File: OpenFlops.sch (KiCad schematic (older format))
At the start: 82 parts, among them J99 OSHW_LOGO, P1 FLOPPY_CONN, P2 POWER_INPUT, P3 USB_A_FEMALE, P4 PROG_PORT, P5 JUMPERS, P6 ENCODER_PORT, P7 DISPLAY_PORT, P8 USB_HEADER, P9 EXTERNAL_SPEAKER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

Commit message: Fix #4
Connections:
- net GND: now also U3.28 (PB2)
- no-connect marks 22 -> 21
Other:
- moved on the sheet: P9
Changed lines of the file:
@@
 NoConn ~ 3255 1900
 NoConn ~ 3255 2600
-NoConn ~ 3255 3200
 NoConn ~ 1855 2800
 NoConn ~ 1855 3900
@@
 L Connector_Generic:Conn_01x02 P9
 U 1 1 5D86073A
-P 4235 3670
-F 0 "P9" H 4153 3887 50  0000 C CNN
-F 1 "EXTERNAL_SPEAKER" H 4153 3796 50  0000 C CNN
-F 2 "OpenFlops:PinHeader_1x02_P2.54mm_Mute" H 4235 3670 50  0001 C CNN
-F 3 "~" H 4235 3670 50  0001 C CNN
-	1    4235 3670
+P 4235 3755
+F 0 "P9" H 4153 3972 50  0000 C CNN
+F 1 "EXTERNAL_SPEAKER" H 4153 3881 50  0000 C CNN
+F 2 "OpenFlops:PinHeader_1x02_P2.54mm_Mute" H 4235 3755 50  0001 C CNN
+F 3 "~" H 4235 3755 50  0001 C CNN
+	1    4235 3755
 	-1   0    0    -1
 $EndComp
 Wire Wire Line
-	4435 3670 4680 3670
-Wire Wire Line
-	4435 3770 4680 3770
+	4435 3755 4680 3755
+Wire Wire Line
+	4435 3855 4680 3855
 Wire Wire Line
 	4650 4435 4650 4395
@@
 Text Label 4650 4435 0    50   ~ 0
 spk-
-Text Label 4680 3770 2    50   ~ 0
+Text Label 4680 3855 2    50   ~ 0
 spk-
 Text Label 4650 4060 0    50   ~ 0
 spk+
-Text Label 4680 3670 2    50   ~ 0
+Text Label 4680 3755 2    50   ~ 0
 spk+
 Text Label 7495 1050 0    50   ~ 0
@@
 	0    1    1    0
 $EndComp
+Text Label 3820 3200 2    50   ~ 0
+boot1
+$Comp
+L power:GND #PWR?
+U 1 1 5E2952AE
+P 3950 3250
+F 0 "#PWR?" H 3950 3000 50  0001 C CNN
+F 1 "GND" H 3955 3077 50  0000 C CNN
+F 2 "" H 3950 3250 50  0001 C CNN
+F 3 "" H 3950 3250 50  0001 C CNN
+	1    3950 3250
+	1    0    0    -1
+$EndComp
+Wire Wire Line
+	3950 3200 3950 3250
+Wire Wire Line
+	3255 3200 3950 3200
 $EndSCHEMATC

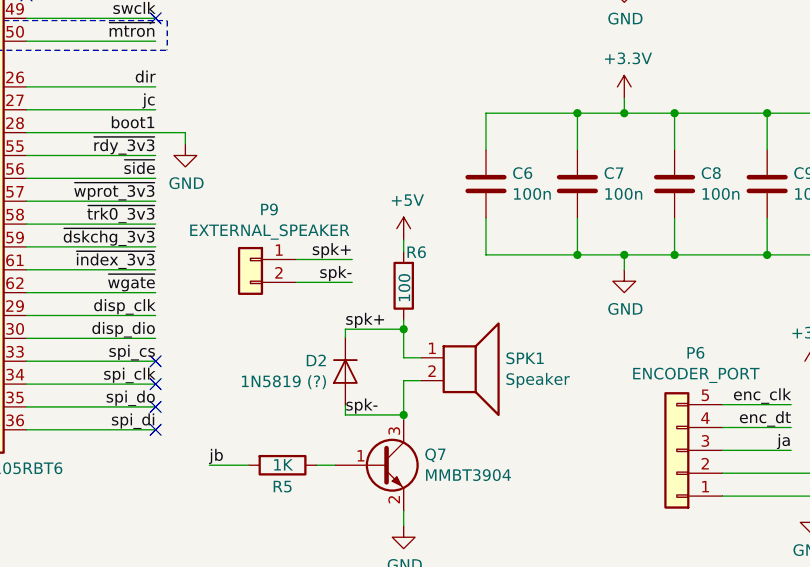
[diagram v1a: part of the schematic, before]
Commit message: Make R6 22R
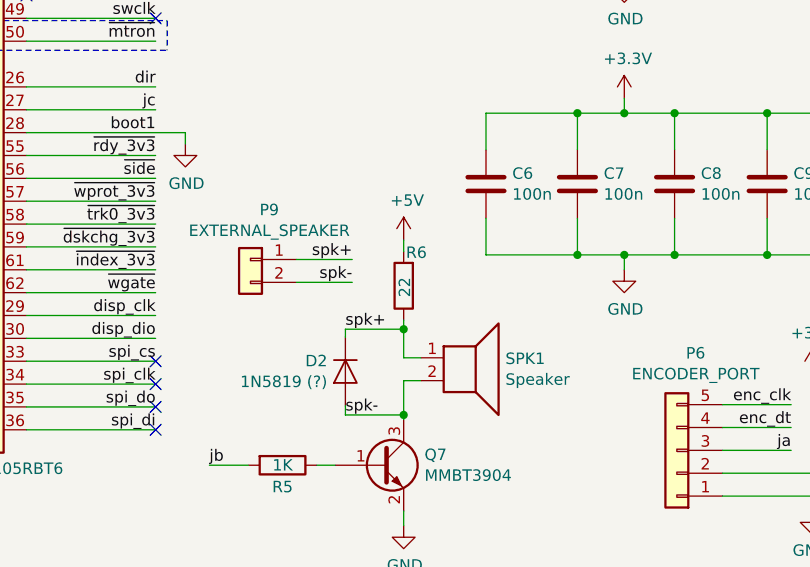
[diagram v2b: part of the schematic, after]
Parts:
- R6: value 100 -> 22
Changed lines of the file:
@@
 P 4905 3870
 F 0 "R6" H 4895 3725 50  0000 R CNN
-F 1 "100" V 4900 3945 50  0000 R CNN
+F 1 "22" V 4900 3920 50  0000 R CNN
 F 2 "Resistor_SMD:R_0805_2012Metric_Pad1.15x1.40mm_HandSolder" V 4835 3870 50  0001 C CNN
 F 3 "~" H 4905 3870 50  0001 C CNN
@@
 boot1
 $Comp
-L power:GND #PWR?
+L power:GND #PWR0146
 U 1 1 5E2952AE
 P 3950 3250
-F 0 "#PWR?" H 3950 3000 50  0001 C CNN
+F 0 "#PWR0146" H 3950 3000 50  0001 C CNN
 F 1 "GND" H 3955 3077 50  0000 C CNN
 F 2 "" H 3950 3250 50  0001 C CNN

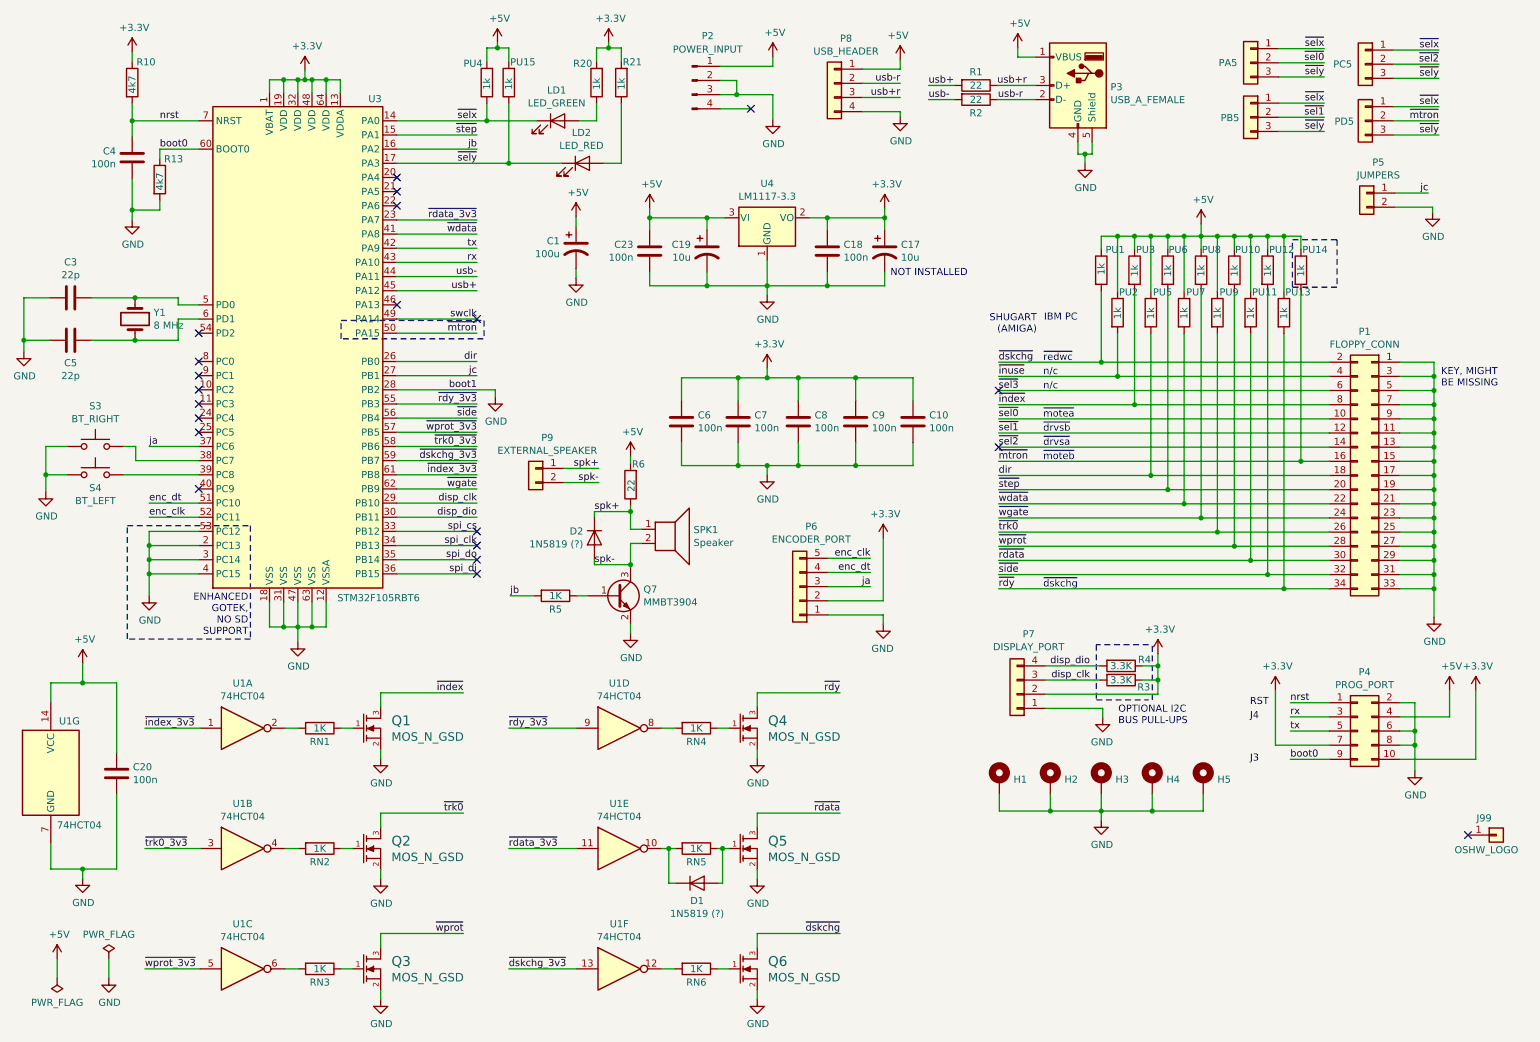
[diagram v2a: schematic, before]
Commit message: Add BOOT1 testpoint and lots of changes for auto P&P
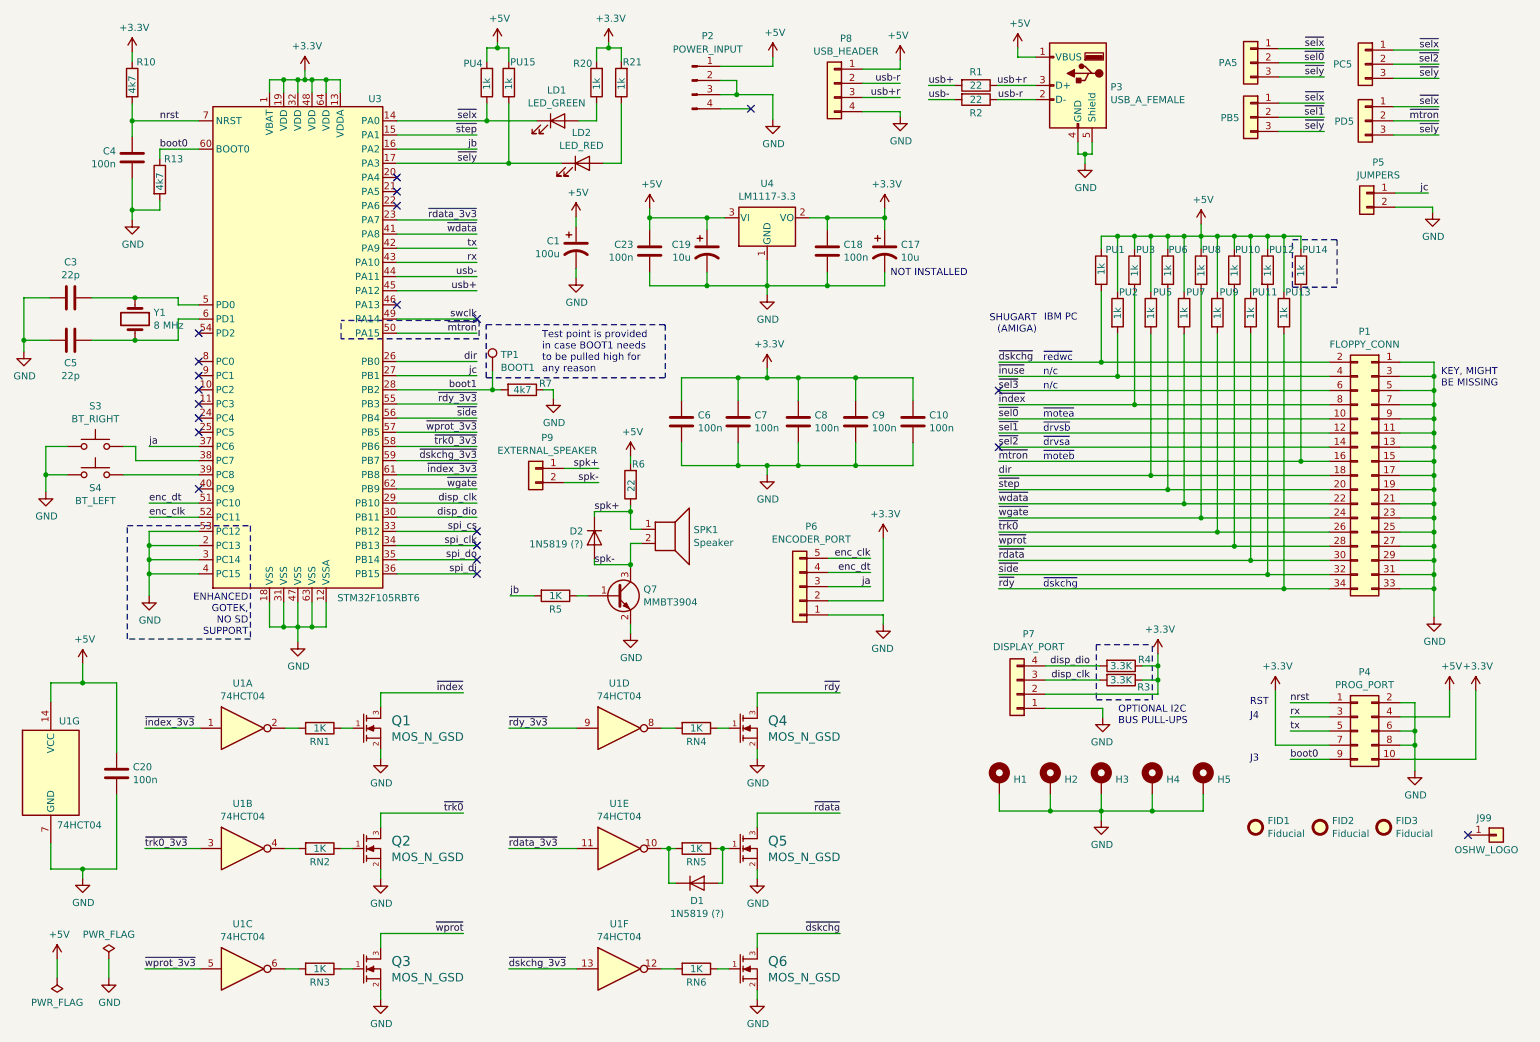
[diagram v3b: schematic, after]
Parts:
- added FID1, FID2, FID3: Fiducial, Fiducial:Fiducial_0.75mm_Mask1.5mm, symbol Mechanical:Fiducial
- added R7: 4k7, Resistor_SMD:R_0805_2012Metric_Pad1.15x1.40mm_HandSolder, symbol Device:R
- added TP1: BOOT1, TestPoint:TestPoint_Pad_D1.5mm, symbol Connector:TestPoint
- C10, C18, C20, C23, C4, C6, C7, C8, C9: JLCPCB PN (none) -> CC0805KRX7R9BB104; MFG Name (none) -> YAGEO; MFG Part Num (none) -> MULTILAYER CERAMIC CAPACITORS MLCC - SMD/SMT 100NF 50V 0805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
- C3, C5: JLCPCB PN (none) -> CL21C220JBANNNC; MFG Name (none) -> SAMSUNG ELECTRO-MECHANICS; MFG Part Num (none) -> MULTILAYER CERAMIC CAPACITORS MLCC - SMD/SMT 22PF 50V 0805 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
- D1, D2: JLCPCB PN (none) -> 1N4148WS; MFG Name (none) -> CHANGJIANG ELECTRONICS TECH (CJ); MFG Part Num (none) -> SWITCHING DIODE 100V 150MA 1.25V @ 150MA 4NS SOD-323 ROHS B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
- PU1, PU10, PU11, PU12, PU13, PU14, PU15, PU2, PU3, PU4, PU5, PU6, PU7, PU8, PU9, RN1, RN2, RN3, RN4, RN5, RN6: JLCPCB PN (none) -> 0805W8F1001T5E; MFG Name (none) -> UNIROYAL ELEC; MFG Part Num (none) -> CHIP RESISTOR - SURFACE MOUNT 1KOHMS ±1% 1/8W 0805 ROHS Bas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
- Q1, Q2, Q3, Q4, Q5, Q6: JLCPCB PN (none) -> BSS138; MFG Name (none) -> ON SEMICON; MFG Part Num (none) -> MOSFET N TRENCH 50V 220MA 1.5V @ 1MA 3.5 ? @ 220MA,10V SOT-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
- Q7: JLCPCB PN (none) -> MMBT3904; MFG Name (none) -> CHANGJIANG ELECTRONICS TECH (CJ); MFG Part Num (none) -> TRANSISTORS (NPN/PNP) NPN 200MA 40V SOT-23(SOT-23-3) ROHS B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
- R1, R2, R6: JLCPCB PN (none) -> 0805W8F220JT5E; MFG Name (none) -> UNIROYAL ELEC; MFG Part Num (none) -> CHIP RESISTOR - SURFACE MOUNT 22OHMS ±1% 1/8W 0805 ROHS Bas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
- R10, R13: JLCPCB PN (none) -> 0805W8F4701T5E; MFG Name (none) -> UNIROYAL ELEC; MFG Part Num (none) -> CHIP RESISTOR - SURFACE MOUNT 4.7KOHMS ±1% 1/8W 0805 ROHS
- U1: JLCPCB PN (none) -> 74HCT04D; MFG Name (none) -> NEXPERIA; MFG Part Num (none) -> GATES AND INVERTERS SOIC-14_150MIL ROHS Extended Part
- U3: JLCPCB PN (none) -> STM32F105RBT6; MFG Name (none) -> STMICROELECTRONICS; MFG Part Num (none) -> ST MICROELECTRONICS LQFP-64_10X10X05P ROHS Extended Part
- U4: JLCPCB PN (none) -> AMS1117-3.3; MFG Name (none) -> ADVANCED MONOLITHIC SYSTEMS; MFG Part Num (none) -> LOW DROPOUT REGULATORS(LDO) POSITIVE FIXED 1.3V @ 800MA 15V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
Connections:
- net GND: now also R7.1; no longer U3.28 (PB2)
- new net boot1: R7.2, TP1.1, U3.28 (PB2)
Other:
- note added: "Test point is provided\nin case BOOT1 needs\nto be pulled high for\nany reason"

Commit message: Some refinements
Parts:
- TP1: footprint TestPoint:TestPoint_Pad_D1.5mm -> TestPoint:TestPoint_Pad_D1.0mm
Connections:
- no-connect marks 21 -> 20
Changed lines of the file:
@@
 	7505 3005 8230 3005
 NoConn ~ 7505 3205
-NoConn ~ 7505 3605
 Text Notes 7820 3105 0    50   ~ 0
 n/c
@@
 F 0 "TP1" H 3988 3188 50  0000 L CNN
 F 1 "BOOT1" H 3988 3097 50  0000 L CNN
-F 2 "TestPoint:TestPoint_Pad_D1.5mm" H 4130 3070 50  0001 C CNN
+F 2 "TestPoint:TestPoint_Pad_D1.0mm" H 4130 3070 50  0001 C CNN
 F 3 "~" H 4130 3070 50  0001 C CNN
 	1    3930 3070

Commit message: Fixes for BOM
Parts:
- D1, D2: value 1N5819 (?) -> 1N4148
- P5: value JUMPERS -> JUMPER_JC
- Q1, Q2, Q3, Q4, Q5, Q6: value MOS_N_GSD -> BSS138
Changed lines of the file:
@@
 P 5375 6685
 F 0 "D1" H 5375 6561 50  0000 C CNN
-F 1 "1N5819 (?)" H 5375 6470 50  0000 C CNN
+F 1 "1N4148" H 5375 6470 50  0000 C CNN
 F 2 "Diode_SMD:D_SOD-323_HandSoldering" H 5375 6685 50  0001 C CNN
 F 3 "~" H 5375 6685 50  0001 C CNN
@@
 P 3040 5590
 F 0 "Q1" H 3216 5643 70  0000 L CNN
-F 1 "MOS_N_GSD" H 3216 5529 60  0000 L CNN
+F 1 "BSS138" H 3216 5529 60  0000 L CNN
 F 2 "Package_TO_SOT_SMD:SOT-23_Handsoldering" H 3040 5590 60  0001 C CNN
 F 3 "" H 3040 5590 60  0000 C CNN
@@
 P 3040 6440
 F 0 "Q2" H 3216 6493 70  0000 L CNN
-F 1 "MOS_N_GSD" H 3216 6379 60  0000 L CNN
+F 1 "BSS138" H 3216 6379 60  0000 L CNN
 F 2 "Package_TO_SOT_SMD:SOT-23_Handsoldering" H 3040 6440 60  0001 C CNN
 F 3 "" H 3040 6440 60  0000 C CNN
@@
 P 3040 7290
 F 0 "Q3" H 3216 7343 70  0000 L CNN
-F 1 "MOS_N_GSD" H 3216 7229 60  0000 L CNN
+F 1 "BSS138" H 3216 7229 60  0000 L CNN
 F 2 "Package_TO_SOT_SMD:SOT-23_Handsoldering" H 3040 7290 60  0001 C CNN
 F 3 "" H 3040 7290 60  0000 C CNN
@@
 P 5700 7290
 F 0 "Q6" H 5876 7343 70  0000 L CNN
-F 1 "MOS_N_GSD" H 5876 7229 60  0000 L CNN
+F 1 "BSS138" H 5876 7229 60  0000 L CNN
 F 2 "Package_TO_SOT_SMD:SOT-23_Handsoldering" H 5700 7290 60  0001 C CNN
 F 3 "" H 5700 7290 60  0000 C CNN
@@
 P 5700 6440
 F 0 "Q5" H 5876 6493 70  0000 L CNN
-F 1 "MOS_N_GSD" H 5876 6379 60  0000 L CNN
+F 1 "BSS138" H 5876 6379 60  0000 L CNN
 F 2 "Package_TO_SOT_SMD:SOT-23_Handsoldering" H 5700 6440 60  0001 C CNN
 F 3 "" H 5700 6440 60  0000 C CNN
@@
 P 5700 5590
 F 0 "Q4" H 5876 5643 70  0000 L CNN
-F 1 "MOS_N_GSD" H 5876 5529 60  0000 L CNN
+F 1 "BSS138" H 5876 5529 60  0000 L CNN
 F 2 "Package_TO_SOT_SMD:SOT-23_Handsoldering" H 5700 5590 60  0001 C CNN
 F 3 "" H 5700 5590 60  0000 C CNN
@@
 P 4650 4245
 F 0 "D2" V 4604 4324 50  0000 L CNN
-F 1 "1N5819 (?)" V 4695 4324 50  0000 L CNN
+F 1 "1N4148" V 4695 4324 50  0000 L CNN
 F 2 "Diode_SMD:D_SOD-323_HandSoldering" H 4650 4245 50  0001 C CNN
 F 3 "~" H 4650 4245 50  0001 C CNN
@@
 P 10105 1810
 F 0 "P5" H 10023 2027 50  0000 C CNN
-F 1 "JUMPERS" H 10023 1936 50  0000 C CNN
+F 1 "JUMPER_JC" H 10023 1936 50  0000 C CNN
 F 2 "OpenFlops:PinHeader_1x02_P2.54mm_Vertical" H 10105 1810 50  0001 C CNN
 F 3 "~" H 10105 1810 50  0001 C CNN
